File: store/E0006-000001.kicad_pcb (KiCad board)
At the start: 2 copper layers, 110 x 73.6 mm, 29 parts, among them J1 Power_IN, J2 Connector, J3 S0 input, J4 Leak sensor, J5 Door reed (NO), J6 Seansor_Header_A, J7 Seansor_Header_B, J8 CAN input from Rasp, U1 TMP117xxDRV, U2 INA226

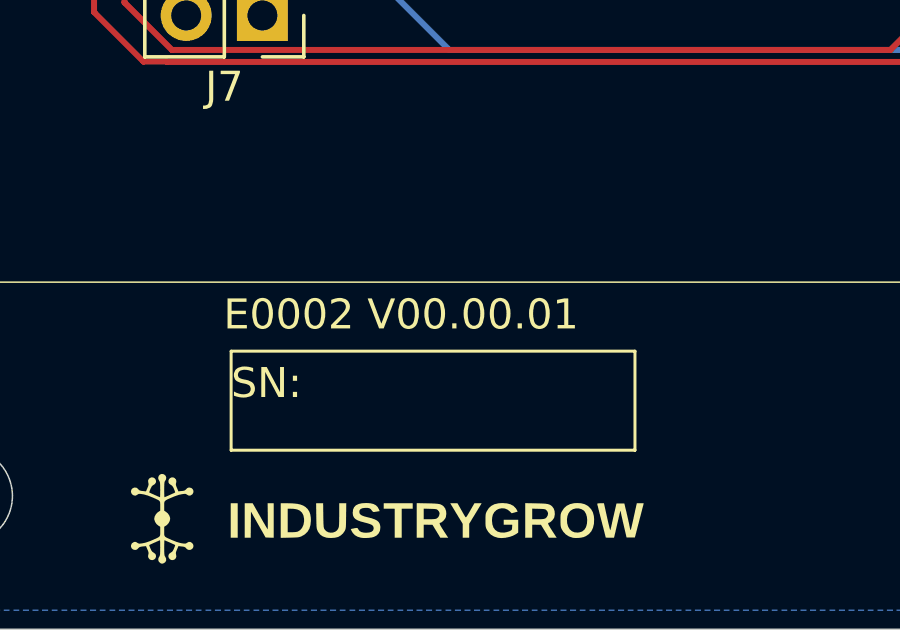
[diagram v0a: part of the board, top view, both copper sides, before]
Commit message: feat(identifiers): add SP-number scheme, registry, and renumber M05-SAFETY
Introduce ADR-0019 (purchased-part SP-number identification) and a
top-level REGISTRY.md mapping E-numbers and SP-numbers to meaning. Renumber
the M05-SAFETY board from E0002 to E0006 so M01-M05 occupy E0002-E0006 in
taxonomy order, and reconcile ADR-0017 to the resolved deferred items.

- ADR-0017: drop duplicated invariant paragraph; condense decision 15 and
  alternative D; record WeAct as an SP part (ADR-0019); resolve the
  registry/store-location deferred item.
- REGISTRY.md: authoritative E-number / SP-number type registry.
- store: rename E0002-000001.* -> E0006-000001.* (KiCad project, render,
  internal sheet/project refs, and silk legend) for the M05-SAFETY design.
- store: carrier E0001 silk-layer fix (F.Paste -> F.SilkS).

Signed-off-by: IIchukissII <133657307+IIchukissII@users.noreply.github.com>
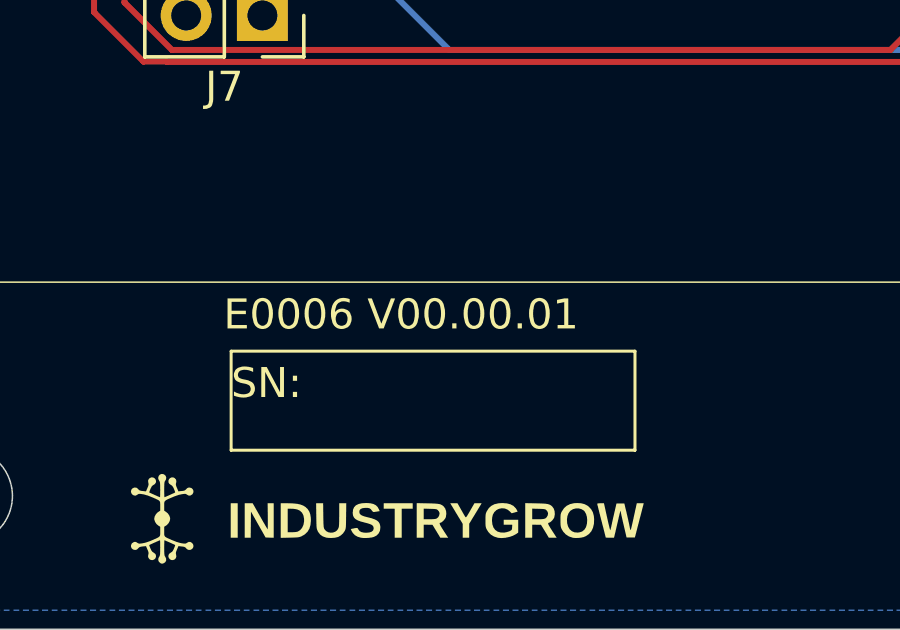
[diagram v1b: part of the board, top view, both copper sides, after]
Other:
- board text added: "E0006 V00.00.01"
- board text removed: "E0002 V00.00.01"
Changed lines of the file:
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@@
 		(property ki_fp_filters "C_*")
 		(sheetname "/")
-		(sheetfile "E0002-000001.kicad_sch")
+		(sheetfile "E0006-000001.kicad_sch")
 		(units
 			(unit
@@
 		(property ki_fp_filters "WSON*1EP?2x2mm?P0.65mm?EP1x1.6mm*")
 		(sheetname "/")
-		(sheetfile "E0002-000001.kicad_sch")
+		(sheetfile "E0006-000001.kicad_sch")
 		(units
 			(unit
@@
 		(property ki_fp_filters "R_*")
 		(sheetname "/")
-		(sheetfile "E0002-000001.kicad_sch")
+		(sheetfile "E0006-000001.kicad_sch")
 		(units
 			(unit
@@
 		(property ki_fp_filters "SOT?23*")
 		(sheetname "/")
-		(sheetfile "E0002-000001.kicad_sch")
+		(sheetfile "E0006-000001.kicad_sch")
 		(units
 			(unit
@@
 		(property ki_fp_filters "C_*")
 		(sheetname "/")
-		(sheetfile "E0002-000001.kicad_sch")
+		(sheetfile "E0006-000001.kicad_sch")
 		(units
 			(unit
@@
 		(property ki_fp_filters "C_*")
 		(sheetname "/")
-		(sheetfile "E0002-000001.kicad_sch")
+		(sheetfile "E0006-000001.kicad_sch")
 		(units
 			(unit
@@
 		(property ki_fp_filters "LED* LED_SMD:* LED_THT:*")
 		(sheetname "/")
-		(sheetfile "E0002-000001.kicad_sch")
+		(sheetfile "E0006-000001.kicad_sch")
 		(units
 			(unit
@@
 		(property ki_fp_filters "R_*")
 		(sheetname "/")
-		(sheetfile "E0002-000001.kicad_sch")
+		(sheetfile "E0006-000001.kicad_sch")
 		(units
 			(unit
@@
 		(property ki_fp_filters "TO-???* *_Diode_* *SingleDiode* D_*")
 		(sheetname "/")
-		(sheetfile "E0002-000001.kicad_sch")
+		(sheetfile "E0006-000001.kicad_sch")
 		(units
 			(unit
@@
 		(property ki_fp_filters "Connector*:*_2x??_*")
 		(sheetname "/")
-		(sheetfile "E0002-000001.kicad_sch")
+		(sheetfile "E0006-000001.kicad_sch")
 		(units
 			(unit
@@
 		(property ki_fp_filters "R_*")
 		(sheetname "/")
-		(sheetfile "E0002-000001.kicad_sch")
+		(sheetfile "E0006-000001.kicad_sch")
 		(units
 			(unit
@@
 		(property ki_fp_filters "Connector*:*_1x??_*")
 		(sheetname "/")
-		(sheetfile "E0002-000001.kicad_sch")
+		(sheetfile "E0006-000001.kicad_sch")
 		(units
 			(unit
@@
 		(property ki_fp_filters "R_*")
 		(sheetname "/")
-		(sheetfile "E0002-000001.kicad_sch")
+		(sheetfile "E0006-000001.kicad_sch")
 		(units
 			(unit
@@
 		(property ki_fp_filters "R_*")
 		(sheetname "/")
-		(sheetfile "E0002-000001.kicad_sch")
+		(sheetfile "E0006-000001.kicad_sch")
 		(units
 			(unit
@@
 		(property ki_fp_filters "Connector*:*_1x??_*")
 		(sheetname "/")
-		(sheetfile "E0002-000001.kicad_sch")
+		(sheetfile "E0006-000001.kicad_sch")
 		(units
 			(unit
@@
 		(property ki_fp_filters "Connector*:*_1x??_*")
 		(sheetname "/")
-		(sheetfile "E0002-000001.kicad_sch")
+		(sheetfile "E0006-000001.kicad_sch")
 		(units
 			(unit
@@
 		(property ki_fp_filters "R_*")
 		(sheetname "/")
-		(sheetfile "E0002-000001.kicad_sch")
+		(sheetfile "E0006-000001.kicad_sch")
 		(units
 			(unit
@@
 		(property ki_fp_filters "*TSSOP*3x3mm?P0.5mm*")
 		(sheetname "/")
-		(sheetfile "E0002-000001.kicad_sch")
+		(sheetfile "E0006-000001.kicad_sch")
 		(units
 			(unit
@@
 		(property ki_fp_filters "R_*")
 		(sheetname "/")
-		(sheetfile "E0002-000001.kicad_sch")
+		(sheetfile "E0006-000001.kicad_sch")
 		(units
 			(unit
@@
 		(property ki_fp_filters "C_*")
 		(sheetname "/")
-		(sheetfile "E0002-000001.kicad_sch")
+		(sheetfile "E0006-000001.kicad_sch")
 		(units
 			(unit
@@
 		(property ki_fp_filters "Connector*:*_1x??_*")
 		(sheetname "/")
-		(sheetfile "E0002-000001.kicad_sch")
+		(sheetfile "E0006-000001.kicad_sch")
 		(units
 			(unit
@@
 		(property ki_fp_filters "Connector*:*_2x??_*")
 		(sheetname "/")
-		(sheetfile "E0002-000001.kicad_sch")
+		(sheetfile "E0006-000001.kicad_sch")
 		(units
 			(unit
@@
 		(property ki_fp_filters "R_*")
 		(sheetname "/")
-		(sheetfile "E0002-000001.kicad_sch")
+		(sheetfile "E0006-000001.kicad_sch")
 		(units
 			(unit
@@
 		(property ki_fp_filters "Connector*:*_1x??_*")
 		(sheetname "/")
-		(sheetfile "E0002-000001.kicad_sch")
+		(sheetfile "E0006-000001.kicad_sch")
 		(units
 			(unit
@@
 		(property ki_fp_filters "C_*")
 		(sheetname "/")
-		(sheetfile "E0002-000001.kicad_sch")
+		(sheetfile "E0006-000001.kicad_sch")
 		(units
 			(unit
@@
 		(property ki_fp_filters "*polyfuse* *PTC*")
 		(sheetname "/")
-		(sheetfile "E0002-000001.kicad_sch")
+		(sheetfile "E0006-000001.kicad_sch")
 		(units
 			(unit
@@
 		(property ki_fp_filters "Connector*:*_1x??_*")
 		(sheetname "/")
-		(sheetfile "E0002-000001.kicad_sch")
+		(sheetfile "E0006-000001.kicad_sch")
 		(units
 			(unit
@@
 		(property ki_fp_filters "R_*")
 		(sheetname "/")
-		(sheetfile "E0002-000001.kicad_sch")
+		(sheetfile "E0006-000001.kicad_sch")
 		(units
 			(unit
@@
 		(layer "Edge.Cuts")
 	)
-	(gr_text "E0002 V00.00.01"
+	(gr_text "E0006 V00.00.01"
 		(at 48.514 98.679 0)
 		(layer "F.SilkS")

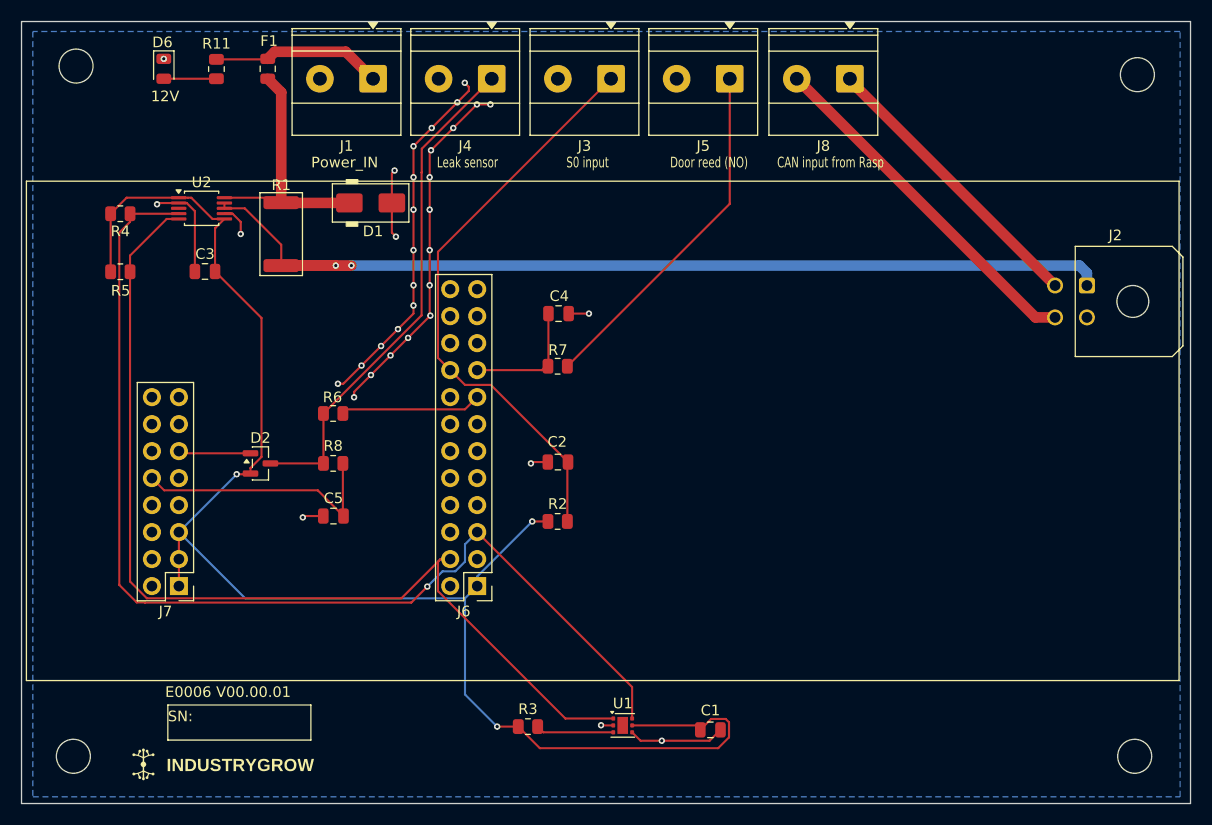
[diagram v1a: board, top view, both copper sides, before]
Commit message: chore(store): update E0006 PCB layout and re-export board render
Revise the E0006 (M05-SAFETY / cabinet distribution + monitoring) board
layout and re-export E0006-000001-D.png. Also adjusts the project file's
default pad geometry (drill/height/width).

Signed-off-by: IIchukissII <133657307+IIchukissII@users.noreply.github.com>
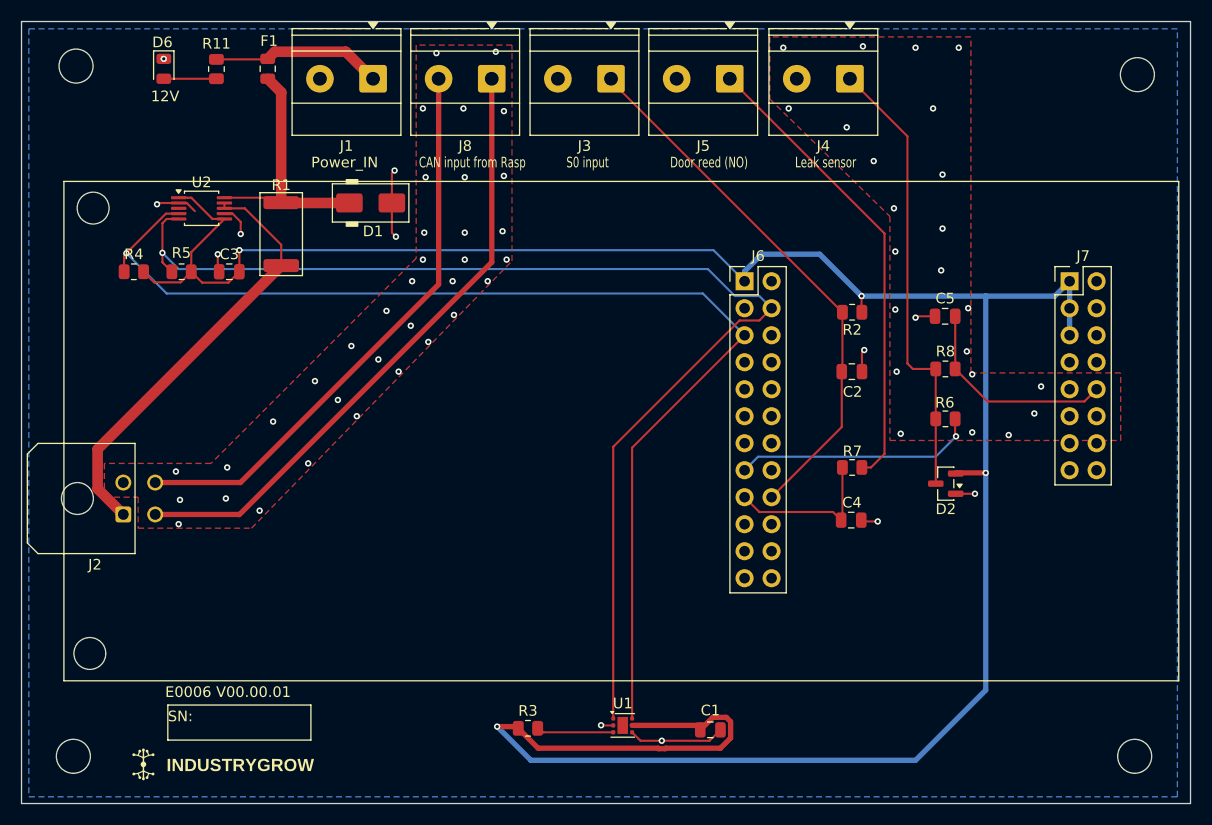
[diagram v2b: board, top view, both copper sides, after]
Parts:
- moved J2 93.2 mm to (44.6, 81.4), turned to 90 degrees
- moved J7 88.6 mm to (133.6, 59.4), turned to 0 degrees
- moved D2 64.5 mm to (122.0, 78.5), turned to 180 degrees
- moved C5 60.6 mm to (121.9, 62.7)
- moved R8 58.3 mm to (121.9, 67.7)
- moved R6 57.6 mm to (121.9, 72.4)
- moved J6 38.2 mm to (103.0, 59.4), turned to 0 degrees
- moved R2 34.0 mm to (113.2, 62.4), turned to 180 degrees
- moved C4 33.7 mm to (113.1, 81.9)
- moved J4 33.7 mm to (113.0, 40.4)
- moved J8 33.7 mm to (79.2, 40.4)
- moved R7 29.3 mm to (113.2, 77.0)
- moved C2 28.9 mm to (113.1, 67.9), turned to 0 degrees
- moved R5 5.76 mm to (50.1, 58.5), turned to 0 degrees
- moved R4 5.61 mm to (45.6, 58.5), turned to 0 degrees
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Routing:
- net STRAP_0: track 146.7 -> 238.7 mm, vias 3 -> 4
- net STRAP_1: track 109.3 -> 32.8 mm, vias 36 -> 70
- net Net-(J2-Pin_1): track 93.2 -> 40.8 mm, vias 2 -> 0
- net CAN_H: track 27.5 -> 58.8 mm
- net CAN_L: track 33.6 -> 53.7 mm
- net I2C1_SCL: track 93.6 -> 112.0 mm, vias 0 -> 1
- net Net-(J5-Pin_1): track 33.4 -> 44.1 mm
- net GPIO_1: track 13.3 -> 22.9 mm, vias 0 -> 1
- net I2C1_SDA: track 101.6 -> 110.1 mm
- net ADC_1: track 24.5 -> 20.0 mm
- net Net-(D2-COM): track 47.7 -> 43.4 mm
- net GPIO_4: track 54.9 -> 51.2 mm
- net GPIO_3: track 11.8 -> 15.0 mm
- added copper zone on F.Cu, net STRAP_1
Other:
- outline, holes or cut-outs redrawn
